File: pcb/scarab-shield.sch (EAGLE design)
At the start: 10 parts

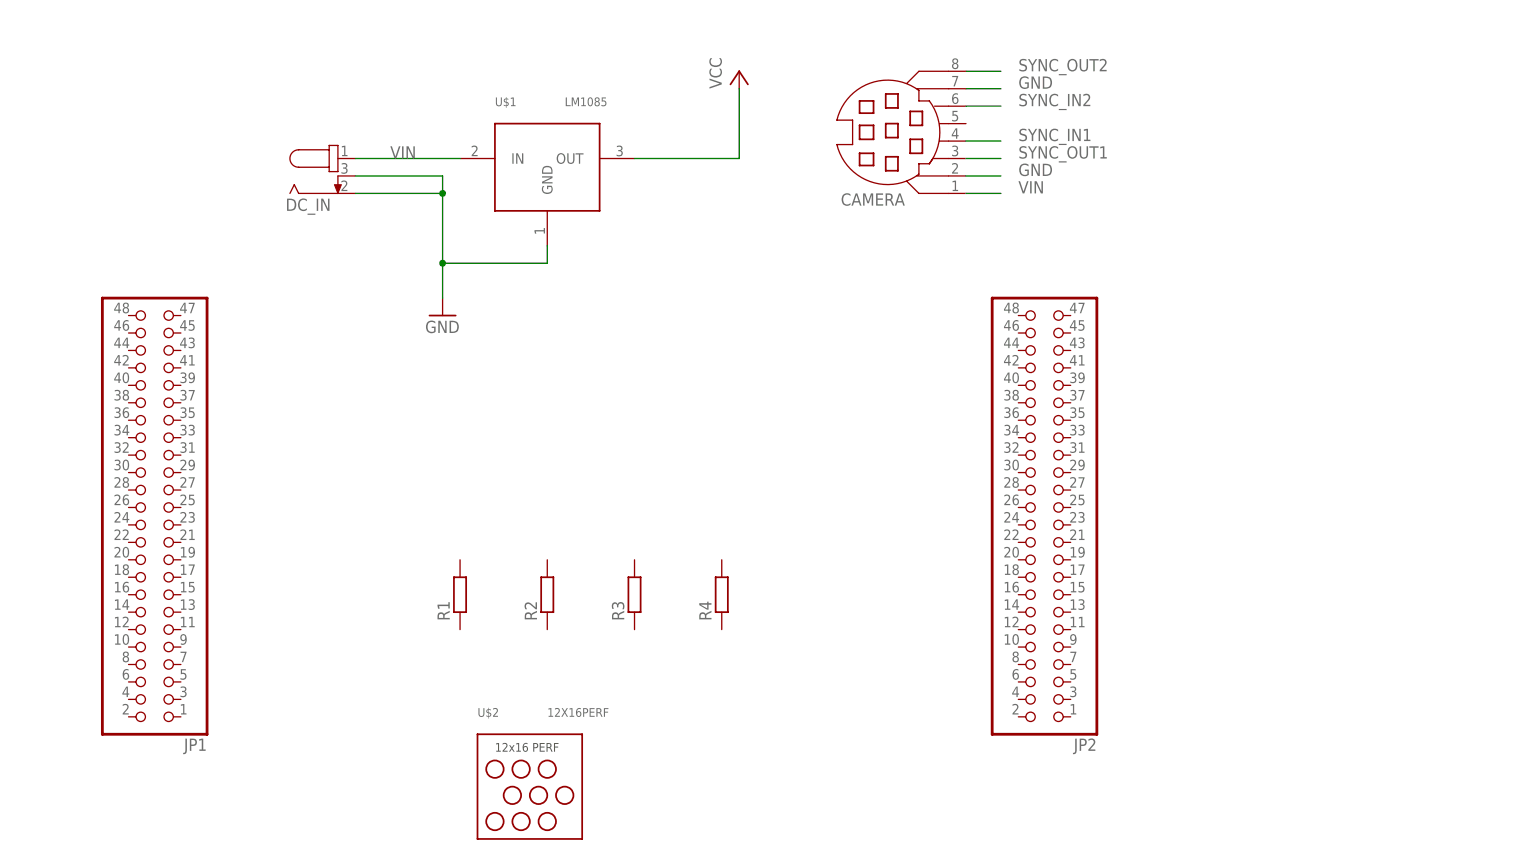
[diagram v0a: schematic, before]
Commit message: finished new camera shield
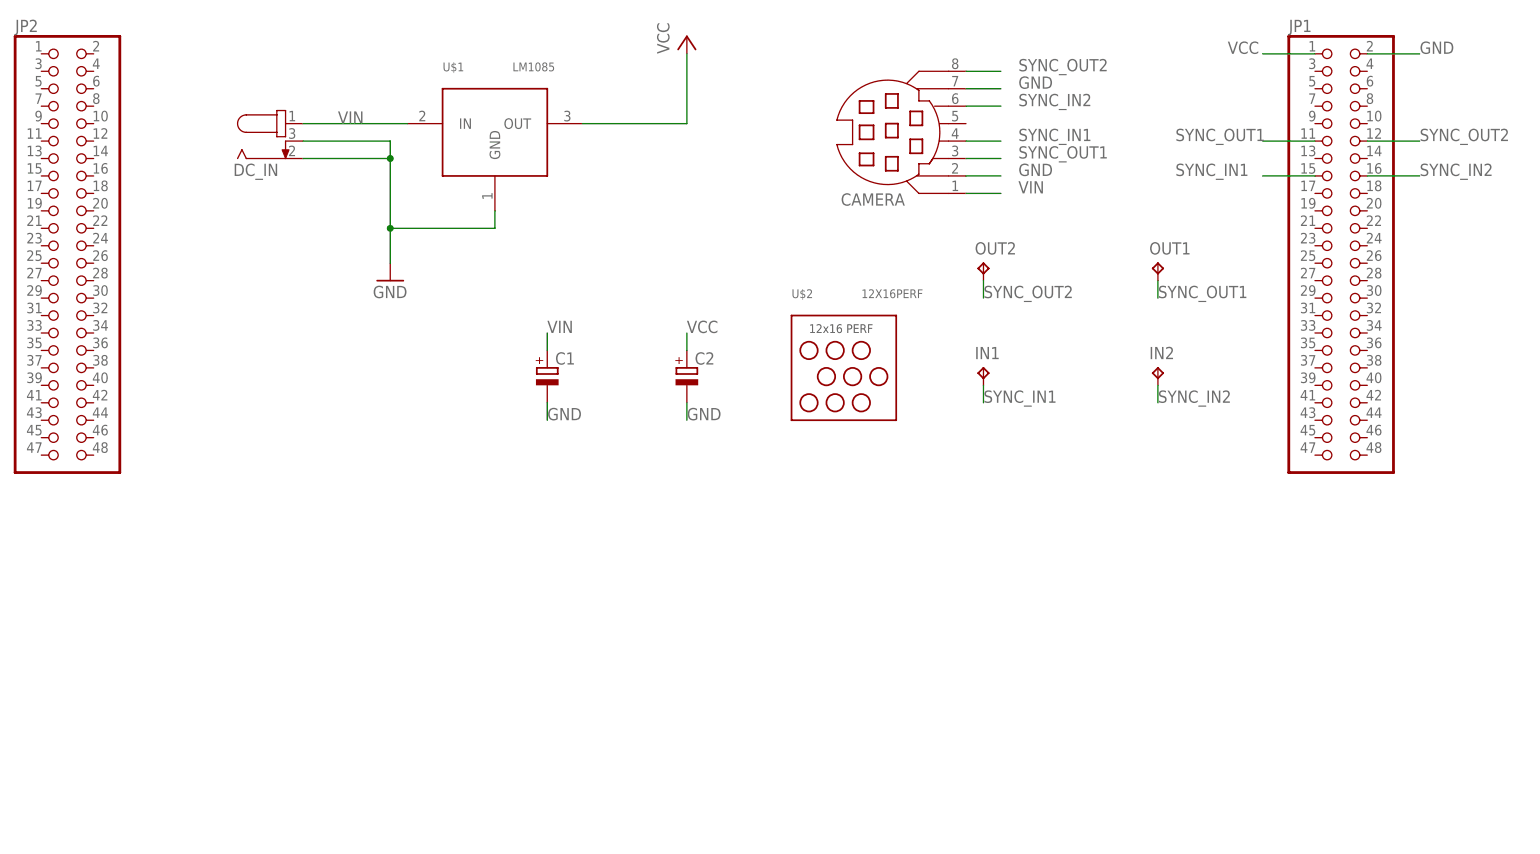
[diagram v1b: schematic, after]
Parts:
- removed R1, R2, R3, R4: (no value), rcl:R-EU_M1206
- added C1, C2: (no value), rcl:CPOL-EUCT7343
- added IN1, IN2, OUT1, OUT2: TPTP20R, testpad:TPTP20R
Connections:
- net GND: now also C1.-, C2.-, JP1.2
- net SYNC_IN1: now also IN1.TP, JP1.15
- net SYNC_IN2: now also IN2.TP, JP1.16
- net SYNC_OUT1: now also JP1.11, OUT1.TP
- net SYNC_OUT2: now also JP1.12, OUT2.TP
- net VCC: now also C2.+, JP1.1
- net VIN: now also C1.+
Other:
- moved on the sheet: DC_IN, JP1, JP2, U$1, U$2
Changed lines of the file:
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@@
 <parts>
 <part name="CAMERA" library="con-yamaichi" library_urn="urn:adsk.eagle:library:202" deviceset="MD08SS" device="" package3d_urn="urn:adsk.eagle:package:11781/1"/>
-<part name="R1" library="rcl" library_urn="urn:adsk.eagle:library:334" deviceset="R-EU_" device="M1206" package3d_urn="urn:adsk.eagle:package:23566/1"/>
-<part name="R2" library="rcl" library_urn="urn:adsk.eagle:library:334" deviceset="R-EU_" device="M1206" package3d_urn="urn:adsk.eagle:package:23566/1"/>
-<part name="R3" library="rcl" library_urn="urn:adsk.eagle:library:334" deviceset="R-EU_" device="M1206" package3d_urn="urn:adsk.eagle:package:23566/1"/>
-<part name="R4" library="rcl" library_urn="urn:adsk.eagle:library:334" deviceset="R-EU_" device="M1206" package3d_urn="urn:adsk.eagle:package:23566/1"/>
 <part name="JP1" library="pinhead" library_urn="urn:adsk.eagle:library:325" deviceset="PINHD-2X24" device="" package3d_urn="urn:adsk.eagle:package:22452/1"/>
 <part name="JP2" library="pinhead" library_urn="urn:adsk.eagle:library:325" deviceset="PINHD-2X24" device="" package3d_urn="urn:adsk.eagle:package:22452/1"/>
@@
 <part name="P+1" library="supply1" library_urn="urn:adsk.eagle:library:371" deviceset="VCC" device=""/>
 <part name="U$2" library="custom-regs" deviceset="12X16PERF" device=""/>
+<part name="C1" library="rcl" library_urn="urn:adsk.eagle:library:334" deviceset="CPOL-EU" device="CT7343" package3d_urn="urn:adsk.eagle:package:23304/2"/>
+<part name="C2" library="rcl" library_urn="urn:adsk.eagle:library:334" deviceset="CPOL-EU" device="CT7343" package3d_urn="urn:adsk.eagle:package:23304/2"/>
+<part name="OUT2" library="testpad" library_urn="urn:adsk.eagle:library:385" deviceset="TP" device="TP20R" package3d_urn="urn:adsk.eagle:package:27973/1" value="TPTP20R"/>
+<part name="OUT1" library="testpad" library_urn="urn:adsk.eagle:library:385" deviceset="TP" device="TP20R" package3d_urn="urn:adsk.eagle:package:27973/1" value="TPTP20R"/>
+<part name="IN1" library="testpad" library_urn="urn:adsk.eagle:library:385" deviceset="TP" device="TP20R" package3d_urn="urn:adsk.eagle:package:27973/1" value="TPTP20R"/>
+<part name="IN2" library="testpad" library_urn="urn:adsk.eagle:library:385" deviceset="TP" device="TP20R" package3d_urn="urn:adsk.eagle:package:27973/1" value="TPTP20R"/>
 </parts>
 <sheets>
@@
 <instances>
 <instance part="CAMERA" gate="G$1" x="129.54" y="114.3" rot="R180"/>
-<instance part="R1" gate="G$1" x="66.04" y="45.72" rot="R90"/>
-<instance part="R2" gate="G$1" x="78.74" y="45.72" rot="R90"/>
-<instance part="R3" gate="G$1" x="91.44" y="45.72" rot="R90"/>
-<instance part="R4" gate="G$1" x="104.14" y="45.72" rot="R90"/>
-<instance part="JP1" gate="A" x="22.86" y="55.88" rot="R180"/>
-<instance part="JP2" gate="A" x="152.4" y="55.88" rot="R180"/>
-<instance part="DC_IN" gate="G$1" x="50.8" y="109.22" smashed="yes">
-<attribute name="NAME" x="40.64" y="101.6" size="1.778" layer="95"/>
+<instance part="JP1" gate="A" x="193.04" y="96.52"/>
+<instance part="JP2" gate="A" x="7.62" y="96.52"/>
+<instance part="DC_IN" gate="G$1" x="43.18" y="114.3" smashed="yes">
+<attribute name="NAME" x="33.02" y="106.68" size="1.778" layer="95"/>
 </instance>
-<instance part="U$1" gate="LM1085" x="71.12" y="114.3"/>
-<instance part="GND1" gate="1" x="63.5" y="86.36"/>
-<instance part="P+1" gate="VCC" x="106.68" y="121.92"/>
-<instance part="U$2" gate="G$1" x="86.36" y="12.7"/>
+<instance part="U$1" gate="LM1085" x="63.5" y="119.38"/>
+<instance part="GND1" gate="1" x="55.88" y="91.44"/>
+<instance part="P+1" gate="VCC" x="99.06" y="127"/>
+<instance part="U$2" gate="G$1" x="132.08" y="73.66"/>
+<instance part="C1" gate="G$1" x="78.74" y="78.74"/>
+<instance part="C2" gate="G$1" x="99.06" y="78.74"/>
+<instance part="OUT2" gate="G$1" x="142.24" y="93.98"/>
+<instance part="OUT1" gate="G$1" x="167.64" y="93.98"/>
+<instance part="IN1" gate="G$1" x="142.24" y="78.74"/>
+<instance part="IN2" gate="G$1" x="167.64" y="78.74"/>
 </instances>
 <busses>
@@
 <pinref part="DC_IN" gate="G$1" pin="1"/>
 <pinref part="U$1" gate="LM1085" pin="IN"/>
-<wire x1="50.8" y1="109.22" x2="66.04" y2="109.22" width="0.1524" layer="91"/>
-<label x="55.88" y="109.22" size="1.778" layer="95"/>
+<wire x1="43.18" y1="114.3" x2="58.42" y2="114.3" width="0.1524" layer="91"/>
+<label x="48.26" y="114.3" size="1.778" layer="95"/>
 </segment>
 <segment>
@@
 <label x="147.32" y="104.14" size="1.778" layer="95"/>
 </segment>
+<segment>
+<pinref part="C1" gate="G$1" pin="+"/>
+<wire x1="78.74" y1="81.28" x2="78.74" y2="83.82" width="0.1524" layer="91"/>
+<label x="78.74" y="83.82" size="1.778" layer="95"/>
+</segment>
 </net>
 <net name="GND" class="0">
 <segment>
 <pinref part="DC_IN" gate="G$1" pin="2"/>
-<wire x1="50.8" y1="104.14" x2="63.5" y2="104.14" width="0.1524" layer="91"/>
-<wire x1="63.5" y1="104.14" x2="63.5" y2="93.98" width="0.1524" layer="91"/>
+<wire x1="43.18" y1="109.22" x2="55.88" y2="109.22" width="0.1524" layer="91"/>
+<wire x1="55.88" y1="109.22" x2="55.88" y2="99.06" width="0.1524" layer="91"/>
 <pinref part="U$1" gate="LM1085" pin="GND"/>
-<wire x1="63.5" y1="93.98" x2="78.74" y2="93.98" width="0.1524" layer="91"/>
-<wire x1="78.74" y1="93.98" x2="78.74" y2="96.52" width="0.1524" layer="91"/>
-<wire x1="63.5" y1="93.98" x2="63.5" y2="88.9" width="0.1524" layer="91"/>
+<wire x1="55.88" y1="99.06" x2="71.12" y2="99.06" width="0.1524" layer="91"/>
+<wire x1="71.12" y1="99.06" x2="71.12" y2="101.6" width="0.1524" layer="91"/>
+<wire x1="55.88" y1="99.06" x2="55.88" y2="93.98" width="0.1524" layer="91"/>
 <pinref part="DC_IN" gate="G$1" pin="3"/>
-<wire x1="50.8" y1="106.68" x2="63.5" y2="106.68" width="0.1524" layer="91"/>
-<wire x1="63.5" y1="106.68" x2="63.5" y2="104.14" width="0.1524" layer="91"/>
-<junction x="63.5" y="104.14"/>
-<junction x="63.5" y="93.98"/>
+<wire x1="43.18" y1="111.76" x2="55.88" y2="111.76" width="0.1524" layer="91"/>
+<wire x1="55.88" y1="111.76" x2="55.88" y2="109.22" width="0.1524" layer="91"/>
+<junction x="55.88" y="109.22"/>
+<junction x="55.88" y="99.06"/>
 <pinref part="GND1" gate="1" pin="GND"/>
 </segment>
@@
 <label x="147.32" y="119.38" size="1.778" layer="95"/>
 </segment>
+<segment>
+<pinref part="JP1" gate="A" pin="2"/>
+<wire x1="198.12" y1="124.46" x2="205.74" y2="124.46" width="0.1524" layer="91"/>
+<label x="205.74" y="124.46" size="1.778" layer="95"/>
+</segment>
+<segment>
+<pinref part="C1" gate="G$1" pin="-"/>
+<wire x1="78.74" y1="73.66" x2="78.74" y2="71.12" width="0.1524" layer="91"/>
+<label x="78.74" y="71.12" size="1.778" layer="95"/>
+</segment>
+<segment>
+<pinref part="C2" gate="G$1" pin="-"/>
+<wire x1="99.06" y1="73.66" x2="99.06" y2="71.12" width="0.1524" layer="91"/>
+<label x="99.06" y="71.12" size="1.778" layer="95"/>
+</segment>
 </net>
 <net name="VCC" class="0">
 <segment>
 <pinref part="U$1" gate="LM1085" pin="OUT"/>
-<wire x1="91.44" y1="109.22" x2="106.68" y2="109.22" width="0.1524" layer="91"/>
-<wire x1="106.68" y1="109.22" x2="106.68" y2="119.38" width="0.1524" layer="91"/>
+<wire x1="83.82" y1="114.3" x2="99.06" y2="114.3" width="0.1524" layer="91"/>
+<wire x1="99.06" y1="114.3" x2="99.06" y2="124.46" width="0.1524" layer="91"/>
 <pinref part="P+1" gate="VCC" pin="VCC"/>
+</segment>
+<segment>
+<pinref part="JP1" gate="A" pin="1"/>
+<wire x1="190.5" y1="124.46" x2="182.88" y2="124.46" width="0.1524" layer="91"/>
+<label x="177.8" y="124.46" size="1.778" layer="95"/>
+</segment>
+<segment>
+<pinref part="C2" gate="G$1" pin="+"/>
+<wire x1="99.06" y1="81.28" x2="99.06" y2="83.82" width="0.1524" layer="91"/>
+<label x="99.06" y="83.82" size="1.778" layer="95"/>
 </segment>
 </net>
@@
 <label x="147.32" y="109.22" size="1.778" layer="95"/>
 </segment>
+<segment>
+<pinref part="JP1" gate="A" pin="11"/>
+<wire x1="190.5" y1="111.76" x2="182.88" y2="111.76" width="0.1524" layer="91"/>
+<label x="170.18" y="111.76" size="1.778" layer="95"/>
+</segment>
+<segment>
+<pinref part="OUT1" gate="G$1" pin="TP"/>
+<wire x1="167.64" y1="91.44" x2="167.64" y2="88.9" width="0.1524" layer="91"/>
+<label x="167.64" y="88.9" size="1.778" layer="95"/>
+</segment>
 </net>
 <net name="SYNC_IN1" class="0">
@@
 <wire x1="139.7" y1="111.76" x2="144.78" y2="111.76" width="0.1524" layer="91"/>
 <label x="147.32" y="111.76" size="1.778" layer="95"/>
+</segment>
+<segment>
+<pinref part="JP1" gate="A" pin="15"/>
+<wire x1="190.5" y1="106.68" x2="182.88" y2="106.68" width="0.1524" layer="91"/>
+<label x="170.18" y="106.68" size="1.778" layer="95"/>
+</segment>
+<segment>
+<pinref part="IN1" gate="G$1" pin="TP"/>
+<wire x1="142.24" y1="76.2" x2="142.24" y2="73.66" width="0.1524" layer="91"/>
+<label x="142.24" y="73.66" size="1.778" layer="95"/>
 </segment>
 </net>
@@
 <label x="147.32" y="116.84" size="1.778" layer="95"/>
 </segment>
+<segment>
+<pinref part="JP1" gate="A" pin="16"/>
+<wire x1="198.12" y1="106.68" x2="205.74" y2="106.68" width="0.1524" layer="91"/>
+<label x="205.74" y="106.68" size="1.778" layer="95"/>
+</segment>
+<segment>
+<pinref part="IN2" gate="G$1" pin="TP"/>
+<wire x1="167.64" y1="76.2" x2="167.64" y2="73.66" width="0.1524" layer="91"/>
+<label x="167.64" y="73.66" size="1.778" layer="95"/>
+</segment>
 </net>
 <net name="SYNC_OUT2" class="0">
@@
 <label x="147.32" y="121.92" size="1.778" layer="95"/>
 </segment>
+<segment>
+<pinref part="JP1" gate="A" pin="12"/>
+<wire x1="198.12" y1="111.76" x2="205.74" y2="111.76" width="0.1524" layer="91"/>
+<label x="205.74" y="111.76" size="1.778" layer="95"/>
+</segment>
+<segment>
+<pinref part="OUT2" gate="G$1" pin="TP"/>
+<wire x1="142.24" y1="91.44" x2="142.24" y2="88.9" width="0.1524" layer="91"/>
+<label x="142.24" y="88.9" size="1.778" layer="95"/>
+</segment>
 </net>
